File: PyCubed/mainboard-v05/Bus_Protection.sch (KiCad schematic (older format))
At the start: 85 parts, among them Q10 MBT2222ADW1T1, Q11 MMDT2907, Q12 BSS138DWQ-7, Q13 BSS138DWQ-7, Q14 BSS138DWQ-7, Q15 MBT2222ADW1T1, Q16 MBT2222ADW1T1, Q17 MMBT2907, Q18 BSS138DWQ-7, Q19 BSS138DWQ-7, Q23 MBT2222ADW1T1, Q24 BSS138DWQ-7, Q25 MBT2222ADW1T1, Q26 BSS138DWQ-7, Q27 MBT2222ADW1T1, Q7 MBT2222ADW1T1, Q8 MBT2222ADW1T1, Q9 BSS138DWQ-7

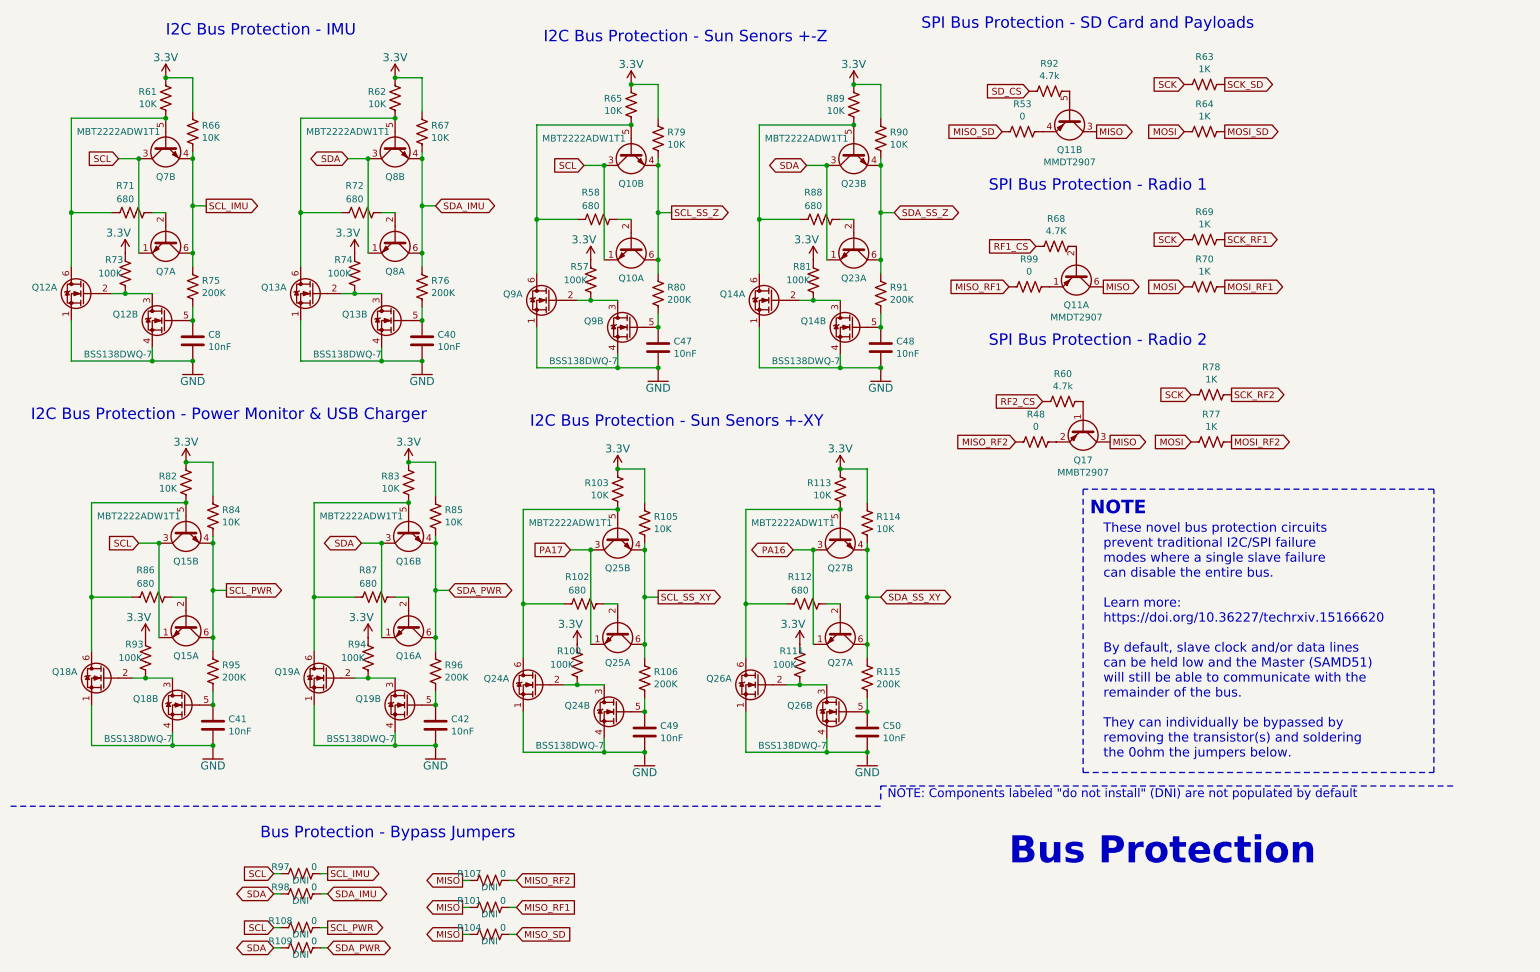
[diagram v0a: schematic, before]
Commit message: Battery board and side panels ready for CAD check and review, pycubed not finished yet
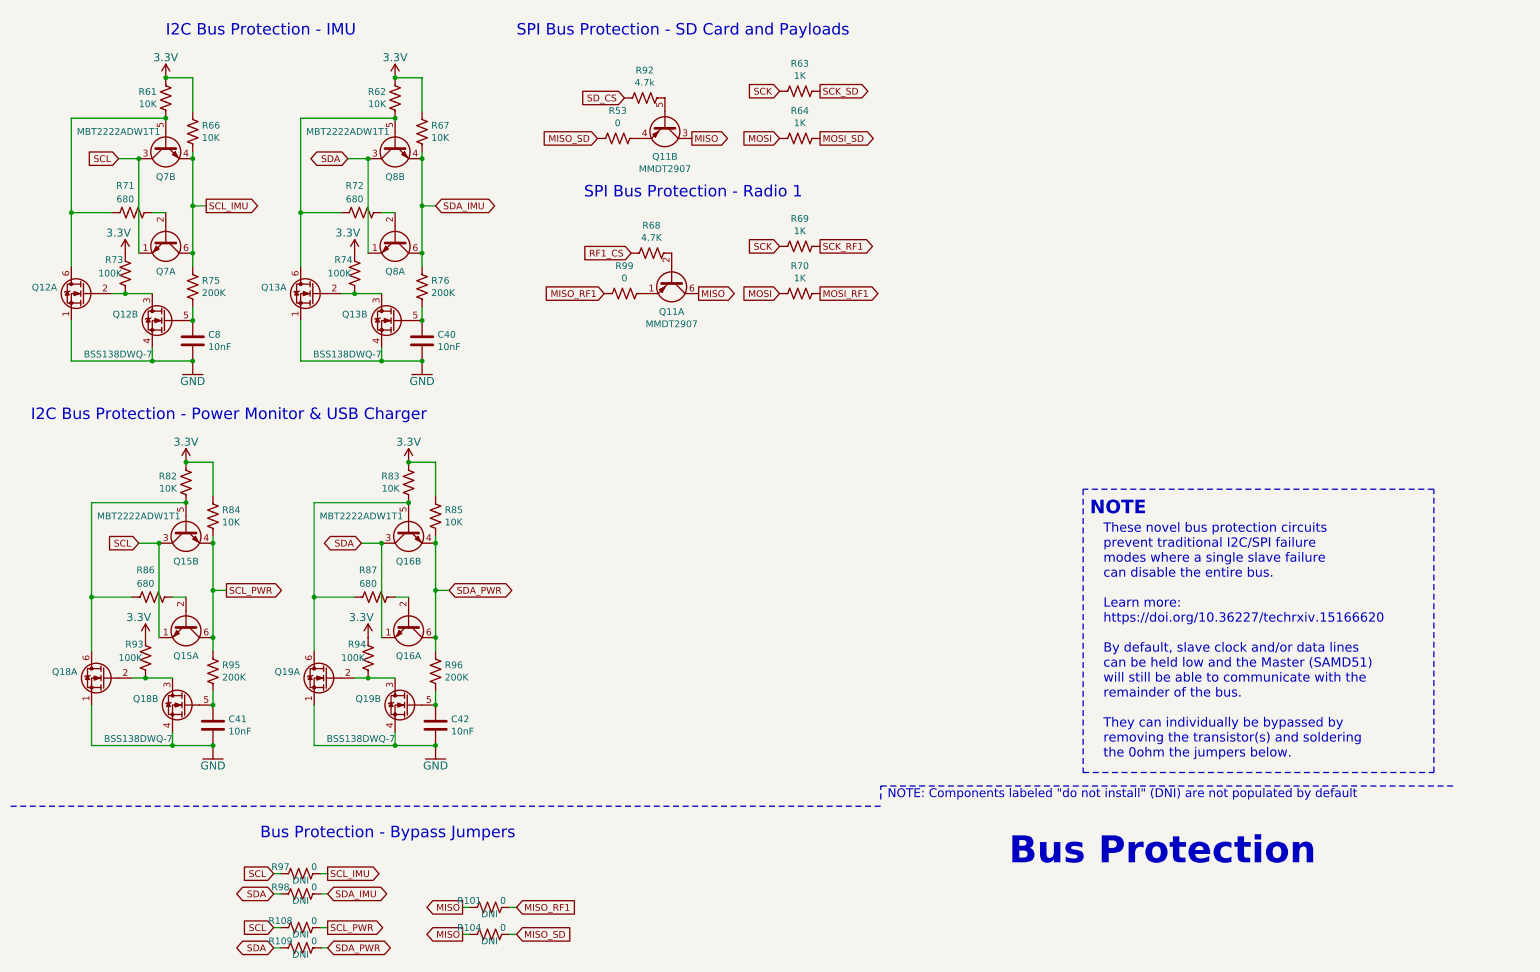
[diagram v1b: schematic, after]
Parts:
- removed C47, C48, C49, C50: 10nF, Capacitor_SMD:C_0603_1608Metric, symbol Device:C
- removed Q10, Q23, Q25, Q27: MBT2222ADW1T1, Package_TO_SOT_SMD:SOT-363_SC-70-6, symbol Transistor_BJT:MBT2222ADW1T1
- removed Q14, Q24, Q26, Q9: BSS138DWQ-7, mainboard:BSS138DWQ-7, symbol mainboard:BSS138DWQ-7
- removed Q17: MMBT2907, Package_TO_SOT_SMD:SOT-23, symbol mainboard:MMBT2907
- removed R100, R111, R57, R81: 100K, Resistor_SMD:R_0603_1608Metric, symbol Device:R_US
- removed R102, R112, R58, R88: 680, Resistor_SMD:R_0603_1608Metric, symbol Device:R_US
- removed R103, R105, R113, R114, R65, R79, R89, R90: 10K, Resistor_SMD:R_0603_1608Metric, symbol Device:R_US
- removed R106, R115, R80, R91: 200K, Resistor_SMD:R_0603_1608Metric, symbol Device:R_US
- removed R107, R48: 0, Resistor_SMD:R_0603_1608Metric, symbol Device:R_US
- removed R60: 4.7k, Resistor_SMD:R_0603_1608Metric, symbol Device:R_US
- removed R77, R78: 1K, Resistor_SMD:R_0603_1608Metric, symbol Device:R_US
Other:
- note removed: "I2C Bus Protection - Sun Senors +-XY"
- note removed: "I2C Bus Protection - Sun Senors +-Z"
- note removed: "SPI Bus Protection - Radio 2"
- moved on the sheet: Q11A, Q11B, R53, R63, R64, R68, R69, R70, R92, R99
